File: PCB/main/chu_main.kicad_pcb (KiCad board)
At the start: 2 copper layers, 294 x 100 mm, 111 parts, among them K1 Conn_01x01_Female, K10 Conn_01x01_Female, K11 Conn_01x01_Female, K12 Conn_01x01_Female, K13 Conn_01x01_Female, K14 Conn_01x01_Female, K15 Conn_01x01_Female, K16 Conn_01x01_Female, K17 Conn_01x01_Female, K18 Conn_01x01_Female, K19 Conn_01x01_Female, K2 Conn_01x01_Female, K20 Conn_01x01_Female, K21 Conn_01x01_Female, K22 Conn_01x01_Female, K23 Conn_01x01_Female, K24 Conn_01x01_Female, K25 Conn_01x01_Female, K26 Conn_01x01_Female, K27 Conn_01x01_Female, K28 Conn_01x01_Female, K29 Conn_01x01_Female, K3 Conn_01x01_Female, K30 Conn_01x01_Female, K31 Conn_01x01_Female, K32 Conn_01x01_Female, K4 Conn_01x01_Female, K5 Conn_01x01_Female, K6 Conn_01x01_Female, K7 Conn_01x01_Female, K8 Conn_01x01_Female, K9 Conn_01x01_Female, U0 ChuAcrylic, U1 Pico, U2 PCA9548APW, U3 MPR121QR2_BOARD, U4 MPR121QR2_BOARD, U5 MPR121QR2_BOARD, U8 SN74LV1T34DBV, X1 GP2Y0E03_REAL, X2 GP2Y0E03_REAL, X3 GP2Y0E03_REAL, X4 GP2Y0E03_REAL, X5 GP2Y0E03_REAL

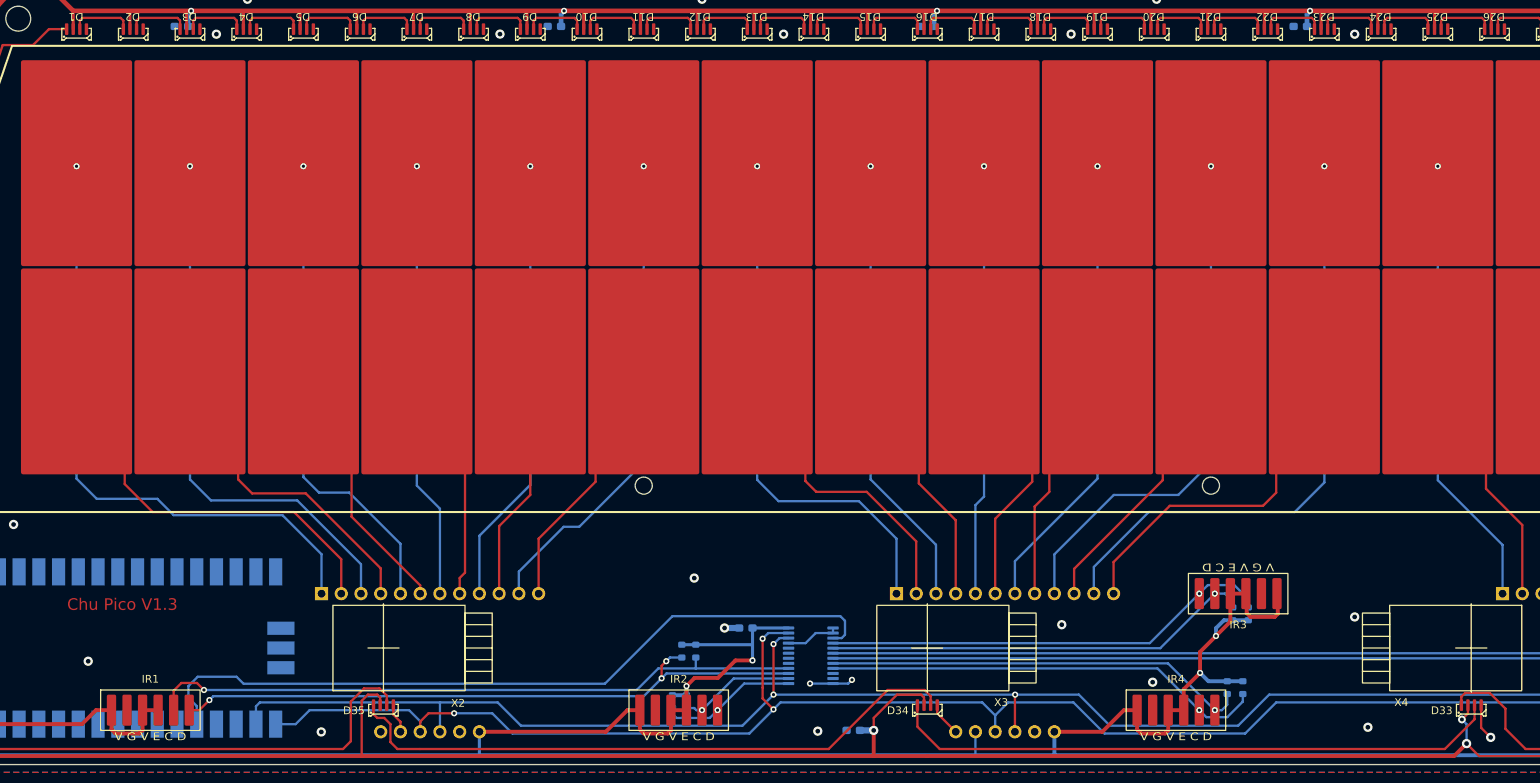
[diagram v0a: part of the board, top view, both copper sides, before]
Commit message: PCB v1.4 (reduce crosstalk)
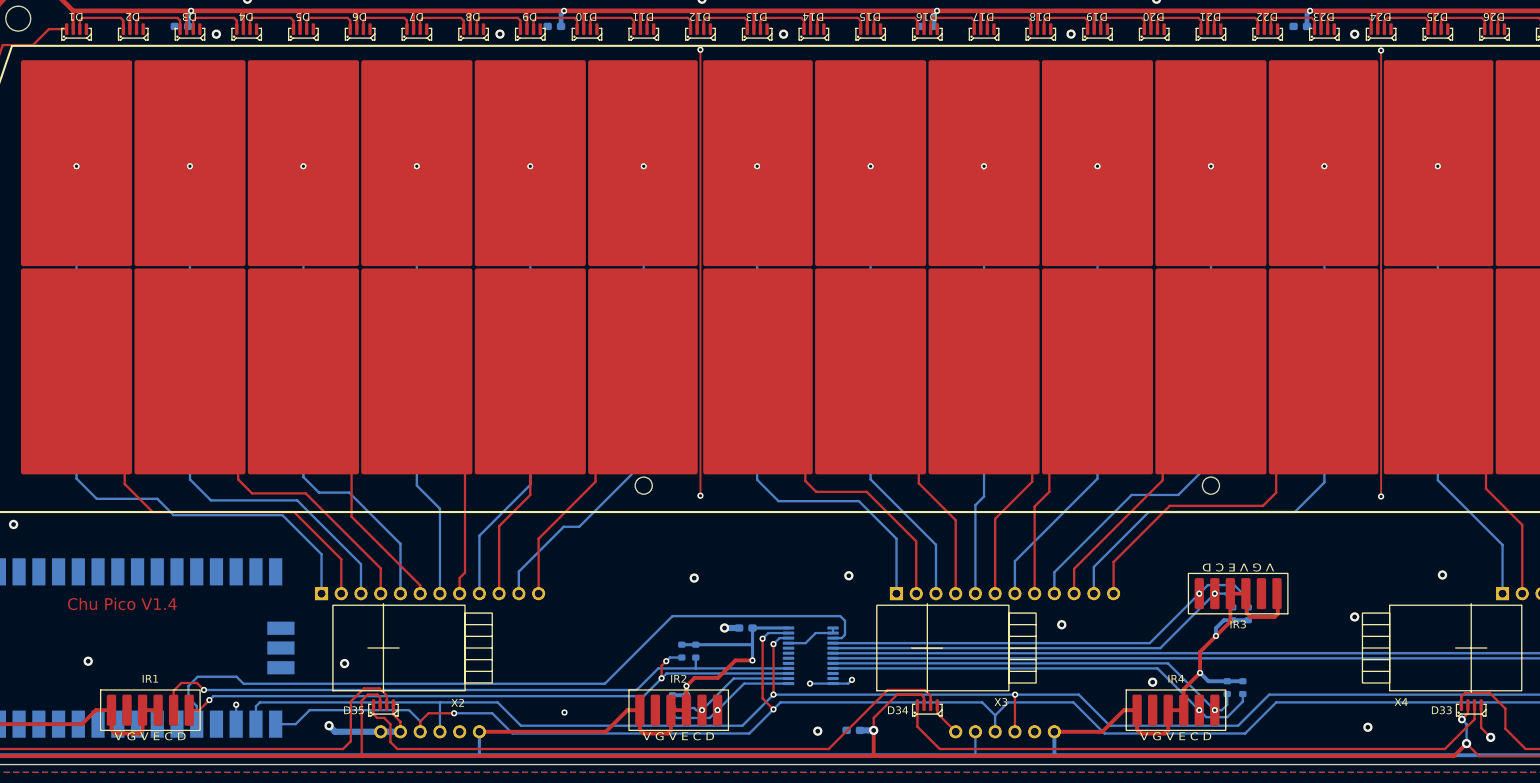
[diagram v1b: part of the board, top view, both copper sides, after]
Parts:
- K11, K14, K23, K26: footprint chu_main:ChuKey -> chu_main:ChuKeyBiasLeft
- K12, K13, K24, K25: footprint chu_main:ChuKey -> chu_main:ChuKeyBiasRight
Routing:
- net GND: track 40.5 -> 167.3 mm, vias 39 -> 48
- net Net-(K21-Pad1): track 68.2 -> 66.9 mm
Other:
- board text added: "Chu Pico V1.4"
- board text removed: "Chu Pico V1.3"

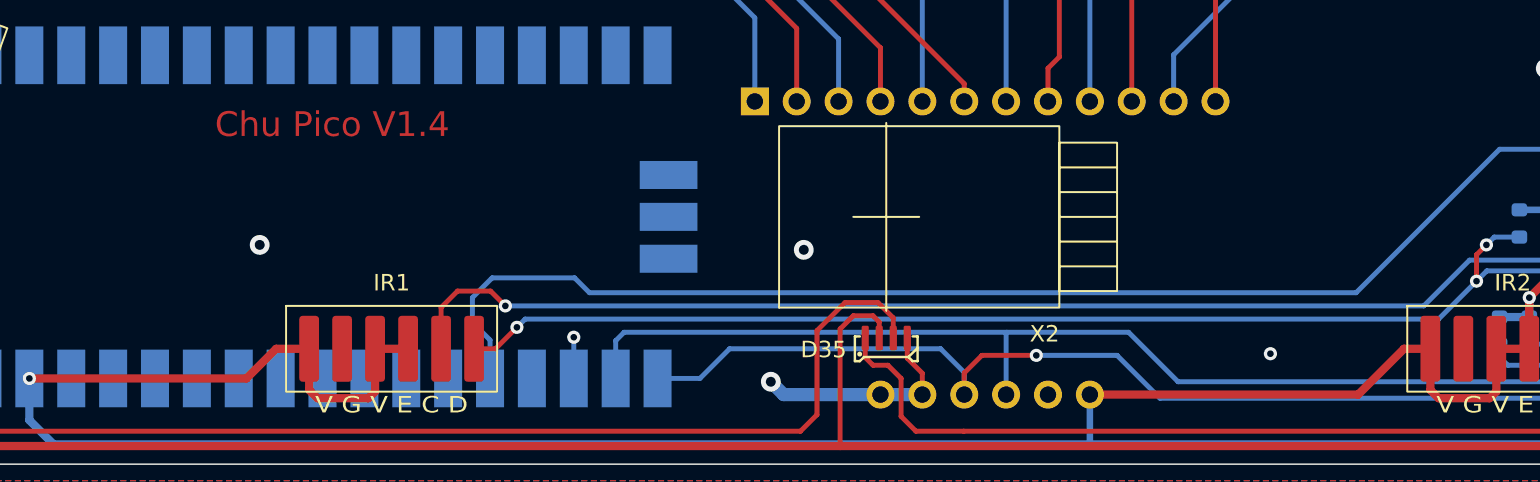
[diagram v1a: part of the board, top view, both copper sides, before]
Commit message: PCB v1.5 for dedicate PN532 pads
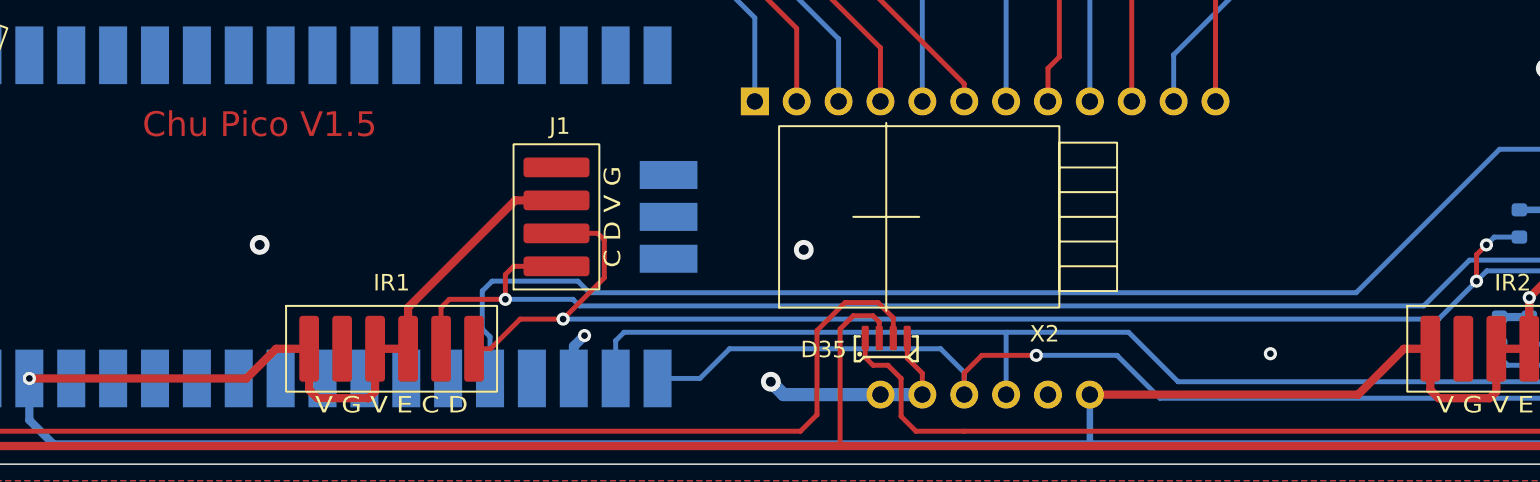
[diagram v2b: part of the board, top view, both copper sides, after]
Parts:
- added J1: Conn_01x04, chu_main:PN532, F.Cu at (124.2, 142.1)
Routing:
- net +3V3: track 429.9 -> 444.1 mm
- net /SDA_1: track 83.7 -> 92.6 mm
- net /SCL_1: track 85.0 -> 89.4 mm
- net Net-(U1-Pad25): track 98.1 -> 97.3 mm
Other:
- board text added: "Chu Pico V1.5"
- board text removed: "Chu Pico V1.4"
